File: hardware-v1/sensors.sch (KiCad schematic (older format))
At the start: 12 parts, among them U13 BMP280, U14 BNO055

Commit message: Footprint work
 - Fix ina219 footprint (for soic)
 - lm4040
 - sn65c1168e -> tssop16
 - sn74hct245 -> tsso20
 - updated bunch of caps to normal 0603 (not handsolder)
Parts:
- C15, C16, C18, C20, C24, C25: footprint Capacitors_SMD:C_0603_HandSoldering -> Capacitors_SMD:C_0603
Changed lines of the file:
@@
 $EndComp
 Wire Wire Line
-	1400 1200 1400 1400
-Wire Wire Line
-	1400 1400 1400 1600
-Wire Wire Line
-	1400 1600 1400 1700
+	1400 1200 1400 1700
 Wire Wire Line
 	1400 1600 1950 1600
 Connection ~ 1400 1400
 $Comp
-L +3.3V #PWR64
+L +3.3V #PWR067
 U 1 1 566E0C88
 P 1400 1200
-F 0 "#PWR64" H 1400 1050 50  0001 C CNN
+F 0 "#PWR067" H 1400 1050 50  0001 C CNN
 F 1 "+3.3V" H 1400 1340 50  0000 C CNN
 F 2 "" H 1400 1200 60  0000 C CNN
@@
 F 0 "C20" H 1760 1870 50  0000 L CNN
 F 1 ".1uF" H 1760 1720 50  0000 L CNN
-F 2 "Capacitors_SMD:C_0603_HandSoldering" H 1750 1800 60  0001 C CNN
+F 2 "Capacitors_SMD:C_0603" H 1750 1800 60  0001 C CNN
 F 3 "" H 1750 1800 60  0000 C CNN
 	1    1750 1800
@@
 F 0 "C18" H 1410 1870 50  0000 L CNN
 F 1 ".1uF" H 1410 1720 50  0000 L CNN
-F 2 "Capacitors_SMD:C_0603_HandSoldering" H 1400 1800 60  0001 C CNN
+F 2 "Capacitors_SMD:C_0603" H 1400 1800 60  0001 C CNN
 F 3 "" H 1400 1800 60  0000 C CNN
 	1    1400 1800
@@
 $EndComp
 Wire Wire Line
-	1750 1200 1750 1400
-Wire Wire Line
-	1750 1400 1750 1700
+	1750 1200 1750 1700
 Connection ~ 1750 1400
 Connection ~ 1400 1600
 Wire Wire Line
-	1400 1900 1400 2000
-Wire Wire Line
-	1400 2000 1400 2100
+	1400 1900 1400 2100
 Wire Wire Line
 	1750 1900 1750 2000
@@
 Connection ~ 1900 2000
 $Comp
-L GND #PWR67
+L GND #PWR068
 U 1 1 566E0CA7
 P 1400 2100
-F 0 "#PWR67" H 1400 1850 50  0001 C CNN
+F 0 "#PWR068" H 1400 1850 50  0001 C CNN
 F 1 "GND" H 1400 1950 50  0000 C CNN
 F 2 "" H 1400 2100 60  0000 C CNN
@@
 	3450 1400 3450 1550
 $Comp
-L GND #PWR66
+L GND #PWR069
 U 1 1 566E0CAF
 P 3450 1550
-F 0 "#PWR66" H 3450 1300 50  0001 C CNN
+F 0 "#PWR069" H 3450 1300 50  0001 C CNN
 F 1 "GND" H 3450 1400 50  0000 C CNN
 F 2 "" H 3450 1550 60  0000 C CNN
@@
 	1550 3300 1550 3250
 Wire Wire Line
-	1550 3250 1650 3250
-Wire Wire Line
-	1650 3250 1800 3250
-$Comp
-L +3.3V #PWR68
+	1550 3250 1800 3250
+$Comp
+L +3.3V #PWR070
 U 1 1 566E0D0B
 P 1650 3200
-F 0 "#PWR68" H 1650 3050 50  0001 C CNN
+F 0 "#PWR070" H 1650 3050 50  0001 C CNN
 F 1 "+3.3V" H 1650 3340 50  0000 C CNN
 F 2 "" H 1650 3200 60  0000 C CNN
@@
 	6450 2050 5950 2050
 Wire Wire Line
-	5950 2050 5950 3200
-Wire Wire Line
-	5950 3200 5950 3500
+	5950 2050 5950 3500
 NoConn ~ 7050 1600
 $Comp
-L GND #PWR69
+L GND #PWR071
 U 1 1 566E19B5
 P 5950 3500
-F 0 "#PWR69" H 5950 3250 50  0001 C CNN
+F 0 "#PWR071" H 5950 3250 50  0001 C CNN
 F 1 "GND" H 5950 3350 50  0000 C CNN
 F 2 "" H 5950 3500 60  0000 C CNN
@@
 	6100 2150 6450 2150
 Wire Wire Line
-	6100 1250 6100 1350
-Wire Wire Line
-	6100 1350 6100 2150
-Wire Wire Line
-	6100 2150 6100 2200
-$Comp
-L +3.3V #PWR65
+	6100 1250 6100 2200
+$Comp
+L +3.3V #PWR072
 U 1 1 566E28E8
 P 6100 1250
-F 0 "#PWR65" H 6100 1100 50  0001 C CNN
+F 0 "#PWR072" H 6100 1100 50  0001 C CNN
 F 1 "+3.3V" H 6100 1390 50  0000 C CNN
 F 2 "" H 6100 1250 60  0000 C CNN
@@
 F 0 "C24" H 6110 2370 50  0000 L CNN
 F 1 ".1uF" H 6110 2220 50  0000 L CNN
-F 2 "Capacitors_SMD:C_0603_HandSoldering" H 6100 2300 60  0001 C CNN
+F 2 "Capacitors_SMD:C_0603" H 6100 2300 60  0001 C CNN
 F 3 "" H 6100 2300 60  0000 C CNN
 	1    6100 2300
@@
 	6300 1350 6300 1550
 Wire Wire Line
-	5800 1350 6100 1350
-Wire Wire Line
-	6100 1350 6300 1350
-Wire Wire Line
-	6300 1350 6500 1350
-Wire Wire Line
-	6500 1350 7150 1350
+	5800 1350 7150 1350
 Connection ~ 6100 1350
 Wire Wire Line
@@
 F 0 "C25" H 7360 3120 50  0000 L CNN
 F 1 ".1uF" H 7360 2970 50  0000 L CNN
-F 2 "Capacitors_SMD:C_0603_HandSoldering" H 7350 3050 60  0001 C CNN
+F 2 "Capacitors_SMD:C_0603" H 7350 3050 60  0001 C CNN
 F 3 "" H 7350 3050 60  0000 C CNN
 	1    7350 3050
@@
 	7450 3200 7450 2800
 Wire Wire Line
-	5950 3200 6100 3200
-Wire Wire Line
-	6100 3200 6450 3200
-Wire Wire Line
-	6450 3200 7050 3200
-Wire Wire Line
-	7050 3200 7350 3200
-Wire Wire Line
-	7350 3200 7450 3200
-Wire Wire Line
-	7450 3200 7950 3200
-Wire Wire Line
-	7950 3200 8550 3200
-Wire Wire Line
-	8550 3200 8950 3200
+	5950 3200 8950 3200
 Wire Wire Line
 	7350 3200 7350 3150
@@
 	7550 2900 7550 2800
 Wire Wire Line
-	5600 2900 5800 2900
-Wire Wire Line
-	5800 2900 7550 2900
+	5600 2900 7550 2900
 NoConn ~ 7650 2800
 NoConn ~ 7750 2800
@@
 	8550 2350 8500 2350
 Wire Wire Line
-	8550 2150 8550 2250
-Wire Wire Line
-	8550 2250 8550 2350
-Wire Wire Line
-	8550 2350 8550 3200
+	8550 2150 8550 3200
 Connection ~ 7950 3200
 Wire Wire Line
@@
 NoConn ~ 7550 1600
 Wire Wire Line
-	7450 1250 7450 1300
-Wire Wire Line
-	7450 1300 7450 1600
+	7450 1250 7450 1600
 Wire Wire Line
 	7450 1300 8950 1300
@@
 F 0 "C15" H 6810 1220 50  0000 L CNN
 F 1 "6.8nF" H 6810 1070 50  0000 L CNN
-F 2 "Capacitors_SMD:C_0603_HandSoldering" H 6800 1150 60  0001 C CNN
+F 2 "Capacitors_SMD:C_0603" H 6800 1150 60  0001 C CNN
 F 3 "" H 6800 1150 60  0000 C CNN
 	1    6800 1150
@@
 F 0 "C16" H 7160 1220 50  0000 L CNN
 F 1 "120nF" H 7160 1070 50  0000 L CNN
-F 2 "Capacitors_SMD:C_0603_HandSoldering" H 7150 1150 60  0001 C CNN
+F 2 "Capacitors_SMD:C_0603" H 7150 1150 60  0001 C CNN
 F 3 "" H 7150 1150 60  0000 C CNN
 	1    7150 1150
@@
 $EndComp
 Wire Wire Line
-	6500 1050 6800 1050
-Wire Wire Line
-	6800 1050 7150 1050
+	6500 1050 7150 1050
 Wire Wire Line
 	6500 1050 6500 1350
@@
 Connection ~ 6800 1050
 Wire Wire Line
-	6800 1250 7150 1250
-Wire Wire Line
-	7150 1250 7450 1250
+	6800 1250 7450 1250
 Connection ~ 7450 1300
 Connection ~ 7150 1250
@@
 NoConn ~ 7350 1600
 Wire Wire Line
-	1400 1400 1750 1400
-Wire Wire Line
-	1750 1400 1950 1400
-Wire Wire Line
-	1400 2000 1750 2000
-Wire Wire Line
-	1750 2000 1900 2000
-Wire Wire Line
-	1900 2000 1950 2000
+	1400 1400 1950 1400
+Wire Wire Line
+	1400 2000 1950 2000
 Wire Wire Line
 	1800 3700 2050 3700

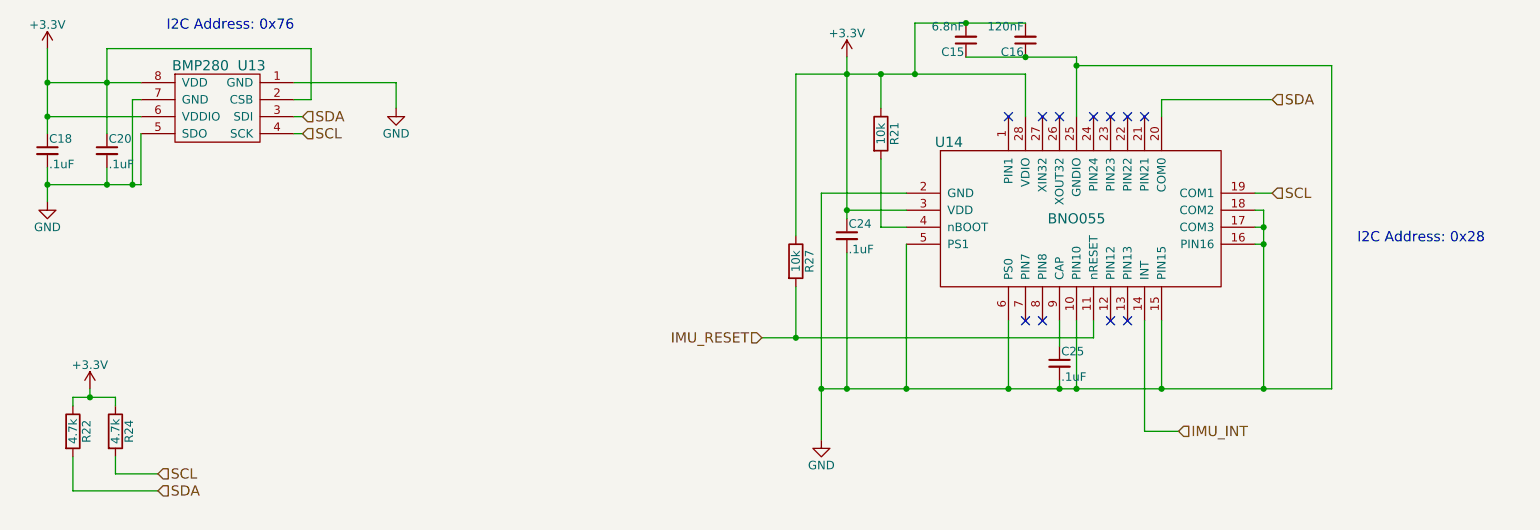
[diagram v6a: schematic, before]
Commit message: First draft of revision B
Lots of changes to the board. Almost completely re-layed out.

Will do some verification now.
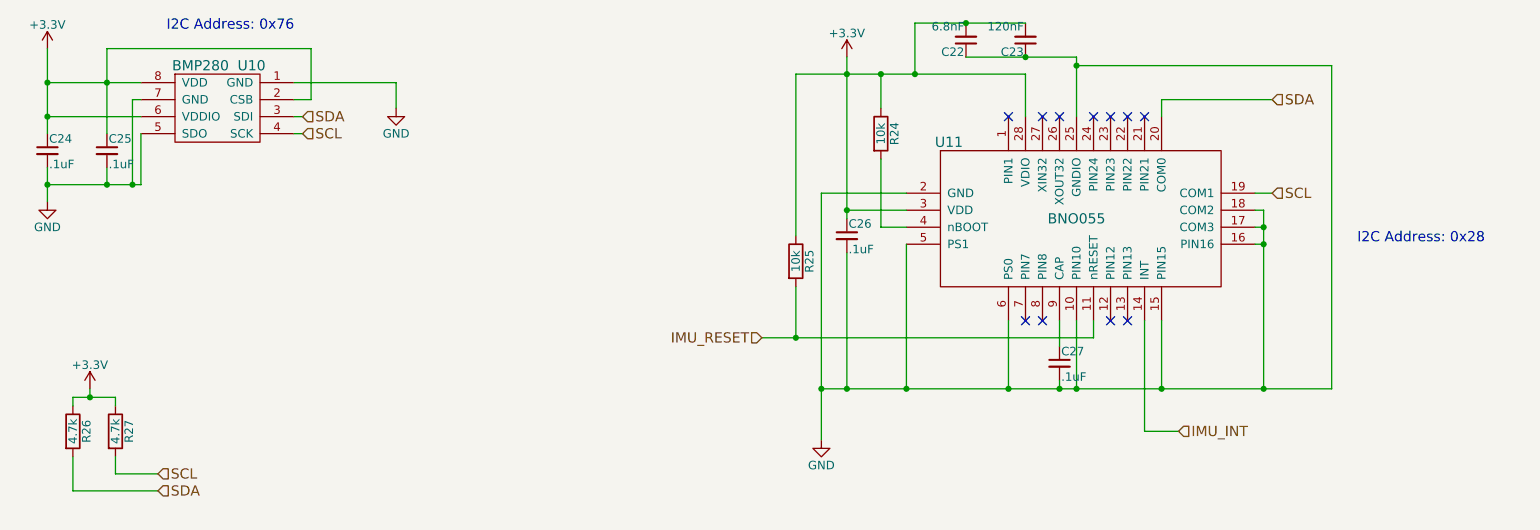
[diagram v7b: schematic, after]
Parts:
- R24: renamed from R21; footprint Resistors_SMD:R_0603_HandSoldering -> Resistors_SMD:R_0603
- R25: renamed from R27; footprint Resistors_SMD:R_0603_HandSoldering -> Resistors_SMD:R_0603
- R26: renamed from R22; footprint Resistors_SMD:R_0603_HandSoldering -> Resistors_SMD:R_0603
- R27: renamed from R24; footprint Resistors_SMD:R_0603_HandSoldering -> Resistors_SMD:R_0603
- renumbered C15 to C22, C16 to C23, C18 to C24, C20 to C25, C24 to C26, C25 to C27, U13 to U10, U14 to U11
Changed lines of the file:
@@
 $EndDescr
 $Comp
-L BMP280 U13
+L BMP280 U10
 U 1 1 566E0C7D
 P 2400 1550
-F 0 "U13" H 2600 1800 60  0000 C CNN
+F 0 "U10" H 2600 1800 60  0000 C CNN
 F 1 "BMP280" H 2300 1800 60  0000 C CNN
 F 2 "bb:BMP280" H 2400 1550 60  0001 C CNN
@@
 Connection ~ 1400 1400
 $Comp
-L +3.3V #PWR067
+L +3.3V #PWR068
 U 1 1 566E0C88
 P 1400 1200
-F 0 "#PWR067" H 1400 1050 50  0001 C CNN
+F 0 "#PWR068" H 1400 1050 50  0001 C CNN
 F 1 "+3.3V" H 1400 1340 50  0000 C CNN
 F 2 "" H 1400 1200 60  0000 C CNN
@@
 $EndComp
 $Comp
-L C_Small C20
+L C_Small C25
 U 1 1 566E0C8E
 P 1750 1800
-F 0 "C20" H 1760 1870 50  0000 L CNN
+F 0 "C25" H 1760 1870 50  0000 L CNN
 F 1 ".1uF" H 1760 1720 50  0000 L CNN
 F 2 "Capacitors_SMD:C_0603" H 1750 1800 60  0001 C CNN
@@
 $EndComp
 $Comp
-L C_Small C18
+L C_Small C24
 U 1 1 566E0C95
 P 1400 1800
-F 0 "C18" H 1410 1870 50  0000 L CNN
+F 0 "C24" H 1410 1870 50  0000 L CNN
 F 1 ".1uF" H 1410 1720 50  0000 L CNN
 F 2 "Capacitors_SMD:C_0603" H 1400 1800 60  0001 C CNN
@@
 Connection ~ 1900 2000
 $Comp
-L GND #PWR068
+L GND #PWR069
 U 1 1 566E0CA7
 P 1400 2100
-F 0 "#PWR068" H 1400 1850 50  0001 C CNN
+F 0 "#PWR069" H 1400 1850 50  0001 C CNN
 F 1 "GND" H 1400 1950 50  0000 C CNN
 F 2 "" H 1400 2100 60  0000 C CNN
@@
 	3450 1400 3450 1550
 $Comp
-L GND #PWR069
+L GND #PWR070
 U 1 1 566E0CAF
 P 3450 1550
-F 0 "#PWR069" H 3450 1300 50  0001 C CNN
+F 0 "#PWR070" H 3450 1300 50  0001 C CNN
 F 1 "GND" H 3450 1400 50  0000 C CNN
 F 2 "" H 3450 1550 60  0000 C CNN
@@
 Connection ~ 1400 2000
 $Comp
-L R R22
+L R R26
 U 1 1 566E0CF6
 P 1550 3450
-F 0 "R22" V 1630 3450 50  0000 C CNN
+F 0 "R26" V 1630 3450 50  0000 C CNN
 F 1 "4.7k" V 1550 3450 50  0000 C CNN
-F 2 "Resistors_SMD:R_0603_HandSoldering" V 1480 3450 30  0001 C CNN
+F 2 "Resistors_SMD:R_0603" V 1480 3450 30  0001 C CNN
 F 3 "" H 1550 3450 30  0000 C CNN
 	1    1550 3450
@@
 $EndComp
 $Comp
-L R R24
+L R R27
 U 1 1 566E0CFD
 P 1800 3450
-F 0 "R24" V 1880 3450 50  0000 C CNN
+F 0 "R27" V 1880 3450 50  0000 C CNN
 F 1 "4.7k" V 1800 3450 50  0000 C CNN
-F 2 "Resistors_SMD:R_0603_HandSoldering" V 1730 3450 30  0001 C CNN
+F 2 "Resistors_SMD:R_0603" V 1730 3450 30  0001 C CNN
 F 3 "" H 1800 3450 30  0000 C CNN
 	1    1800 3450
@@
 	1550 3250 1800 3250
 $Comp
-L +3.3V #PWR070
+L +3.3V #PWR071
 U 1 1 566E0D0B
 P 1650 3200
-F 0 "#PWR070" H 1650 3050 50  0001 C CNN
+F 0 "#PWR071" H 1650 3050 50  0001 C CNN
 F 1 "+3.3V" H 1650 3340 50  0000 C CNN
 F 2 "" H 1650 3200 60  0000 C CNN
@@
 SCL
 $Comp
-L BNO055 U14
+L BNO055 U11
 U 1 1 566E10BF
 P 7500 2200
-F 0 "U14" H 6700 2650 60  0000 C CNN
+F 0 "U11" H 6700 2650 60  0000 C CNN
 F 1 "BNO055" H 7450 2200 60  0000 C CNN
 F 2 "bb:BNO055" H 6900 2350 60  0001 C CNN
@@
 NoConn ~ 7050 1600
 $Comp
-L GND #PWR071
+L GND #PWR072
 U 1 1 566E19B5
 P 5950 3500
-F 0 "#PWR071" H 5950 3250 50  0001 C CNN
+F 0 "#PWR072" H 5950 3250 50  0001 C CNN
 F 1 "GND" H 5950 3350 50  0000 C CNN
 F 2 "" H 5950 3500 60  0000 C CNN
@@
 	6100 1250 6100 2200
 $Comp
-L +3.3V #PWR072
+L +3.3V #PWR073
 U 1 1 566E28E8
 P 6100 1250
-F 0 "#PWR072" H 6100 1100 50  0001 C CNN
+F 0 "#PWR073" H 6100 1100 50  0001 C CNN
 F 1 "+3.3V" H 6100 1390 50  0000 C CNN
 F 2 "" H 6100 1250 60  0000 C CNN
@@
 $EndComp
 $Comp
-L C_Small C24
+L C_Small C26
 U 1 1 566E32A9
 P 6100 2300
-F 0 "C24" H 6110 2370 50  0000 L CNN
+F 0 "C26" H 6110 2370 50  0000 L CNN
 F 1 ".1uF" H 6110 2220 50  0000 L CNN
 F 2 "Capacitors_SMD:C_0603" H 6100 2300 60  0001 C CNN
@@
 	6300 2250 6300 1850
 $Comp
-L R R21
+L R R24
 U 1 1 566E34C5
 P 6300 1700
-F 0 "R21" V 6380 1700 50  0000 C CNN
+F 0 "R24" V 6380 1700 50  0000 C CNN
 F 1 "10k" V 6300 1700 50  0000 C CNN
-F 2 "Resistors_SMD:R_0603_HandSoldering" V 6230 1700 30  0001 C CNN
+F 2 "Resistors_SMD:R_0603" V 6230 1700 30  0001 C CNN
 F 3 "" H 6300 1700 30  0000 C CNN
 	1    6300 1700
@@
 NoConn ~ 7250 2800
 $Comp
-L C_Small C25
+L C_Small C27
 U 1 1 566E365A
 P 7350 3050
-F 0 "C25" H 7360 3120 50  0000 L CNN
+F 0 "C27" H 7360 3120 50  0000 L CNN
 F 1 ".1uF" H 7360 2970 50  0000 L CNN
 F 2 "Capacitors_SMD:C_0603" H 7350 3050 60  0001 C CNN
@@
 Connection ~ 6300 1350
 $Comp
-L C_Small C15
+L C_Small C22
 U 1 1 566E6D3B
 P 6800 1150
-F 0 "C15" H 6810 1220 50  0000 L CNN
+F 0 "C22" H 6810 1220 50  0000 L CNN
 F 1 "6.8nF" H 6810 1070 50  0000 L CNN
 F 2 "Capacitors_SMD:C_0603" H 6800 1150 60  0001 C CNN
@@
 $EndComp
 $Comp
-L C_Small C16
+L C_Small C23
 U 1 1 566E789F
 P 7150 1150
-F 0 "C16" H 7160 1220 50  0000 L CNN
+F 0 "C23" H 7160 1220 50  0000 L CNN
 F 1 "120nF" H 7160 1070 50  0000 L CNN
 F 2 "Capacitors_SMD:C_0603" H 7150 1150 60  0001 C CNN
@@
 Connection ~ 5800 2900
 $Comp
-L R R27
+L R R25
 U 1 1 56A47B87
 P 5800 2450
-F 0 "R27" V 5880 2450 50  0000 C CNN
+F 0 "R25" V 5880 2450 50  0000 C CNN
 F 1 "10k" V 5800 2450 50  0000 C CNN
-F 2 "Resistors_SMD:R_0603_HandSoldering" V 5730 2450 30  0001 C CNN
+F 2 "Resistors_SMD:R_0603" V 5730 2450 30  0001 C CNN
 F 3 "" H 5800 2450 30  0000 C CNN
 	1    5800 2450

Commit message: Finalizing revB
 - Added part numbers on all parts (in kicad PartNumber field)
 - Some finicking in a bunch of corners
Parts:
- C22: PartNumber (none) -> CL10B682KB8SFNC
- C23: PartNumber (none) -> GRM188R71E124KA01D
- C24, C25, C26, C27: PartNumber (none) -> CC0603KPX7R7BB104
- R24, R25: PartNumber (none) -> RC0603JR-0710KL
- R26, R27: PartNumber (none) -> RC0603JR-074K7L
- U10: PartNumber (none) -> BMP280
- U11: PartNumber (none) -> BNO055
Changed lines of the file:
@@
 F 2 "bb:BMP280" H 2400 1550 60  0001 C CNN
 F 3 "" H 2400 1550 60  0000 C CNN
+F 4 "BMP280" H 2400 1550 60  0001 C CNN "PartNumber"
 	1    2400 1550
 	1    0    0    -1
@@
 F 2 "Capacitors_SMD:C_0603" H 1750 1800 60  0001 C CNN
 F 3 "" H 1750 1800 60  0000 C CNN
+F 4 "CC0603KPX7R7BB104" H 1750 1800 60  0001 C CNN "PartNumber"
 	1    1750 1800
 	1    0    0    -1
@@
 F 2 "Capacitors_SMD:C_0603" H 1400 1800 60  0001 C CNN
 F 3 "" H 1400 1800 60  0000 C CNN
+F 4 "CC0603KPX7R7BB104" H 1400 1800 60  0001 C CNN "PartNumber"
 	1    1400 1800
 	1    0    0    -1
@@
 F 2 "Resistors_SMD:R_0603" V 1480 3450 30  0001 C CNN
 F 3 "" H 1550 3450 30  0000 C CNN
+F 4 "RC0603JR-074K7L" V 1550 3450 60  0001 C CNN "PartNumber"
 	1    1550 3450
 	1    0    0    -1
@@
 F 2 "Resistors_SMD:R_0603" V 1730 3450 30  0001 C CNN
 F 3 "" H 1800 3450 30  0000 C CNN
+F 4 "RC0603JR-074K7L" V 1800 3450 60  0001 C CNN "PartNumber"
 	1    1800 3450
 	1    0    0    -1
@@
 F 2 "bb:BNO055" H 6900 2350 60  0001 C CNN
 F 3 "" H 6900 2350 60  0000 C CNN
+F 4 "BNO055" H 7500 2200 60  0001 C CNN "PartNumber"
 	1    7500 2200
 	1    0    0    -1
@@
 F 2 "Capacitors_SMD:C_0603" H 6100 2300 60  0001 C CNN
 F 3 "" H 6100 2300 60  0000 C CNN
+F 4 "CC0603KPX7R7BB104" H 6100 2300 60  0001 C CNN "PartNumber"
 	1    6100 2300
 	1    0    0    -1
@@
 F 2 "Resistors_SMD:R_0603" V 6230 1700 30  0001 C CNN
 F 3 "" H 6300 1700 30  0000 C CNN
+F 4 "RC0603JR-0710KL" V 6300 1700 60  0001 C CNN "PartNumber"
 	1    6300 1700
 	1    0    0    -1
@@
 F 2 "Capacitors_SMD:C_0603" H 7350 3050 60  0001 C CNN
 F 3 "" H 7350 3050 60  0000 C CNN
+F 4 "CC0603KPX7R7BB104" H 7350 3050 60  0001 C CNN "PartNumber"
 	1    7350 3050
 	1    0    0    -1
@@
 F 2 "Capacitors_SMD:C_0603" H 6800 1150 60  0001 C CNN
 F 3 "" H 6800 1150 60  0000 C CNN
+F 4 "CL10B682KB8SFNC" H 6800 1150 60  0001 C CNN "PartNumber"
 	1    6800 1150
 	-1   0    0    1
@@
 F 2 "Capacitors_SMD:C_0603" H 7150 1150 60  0001 C CNN
 F 3 "" H 7150 1150 60  0000 C CNN
+F 4 "GRM188R71E124KA01D" H 7150 1150 60  0001 C CNN "PartNumber"
 	1    7150 1150
 	-1   0    0    1
@@
 F 2 "Resistors_SMD:R_0603" V 5730 2450 30  0001 C CNN
 F 3 "" H 5800 2450 30  0000 C CNN
+F 4 "RC0603JR-0710KL" V 5800 2450 60  0001 C CNN "PartNumber"
 	1    5800 2450
 	1    0    0    -1
